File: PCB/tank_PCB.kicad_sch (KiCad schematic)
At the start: 60 parts, among them J1 TFT, J2 PTSA 1,5/ 2-3,5-Z, J3 PTSA 1,5/ 8-3,5-Z, J5 USB4110GFA, U1 ADS1115IDGS, U3 LM2735X (1.6MHz), U4 ESP32-C6-WROOM-1, U5 MCP1826S-3302E/DB

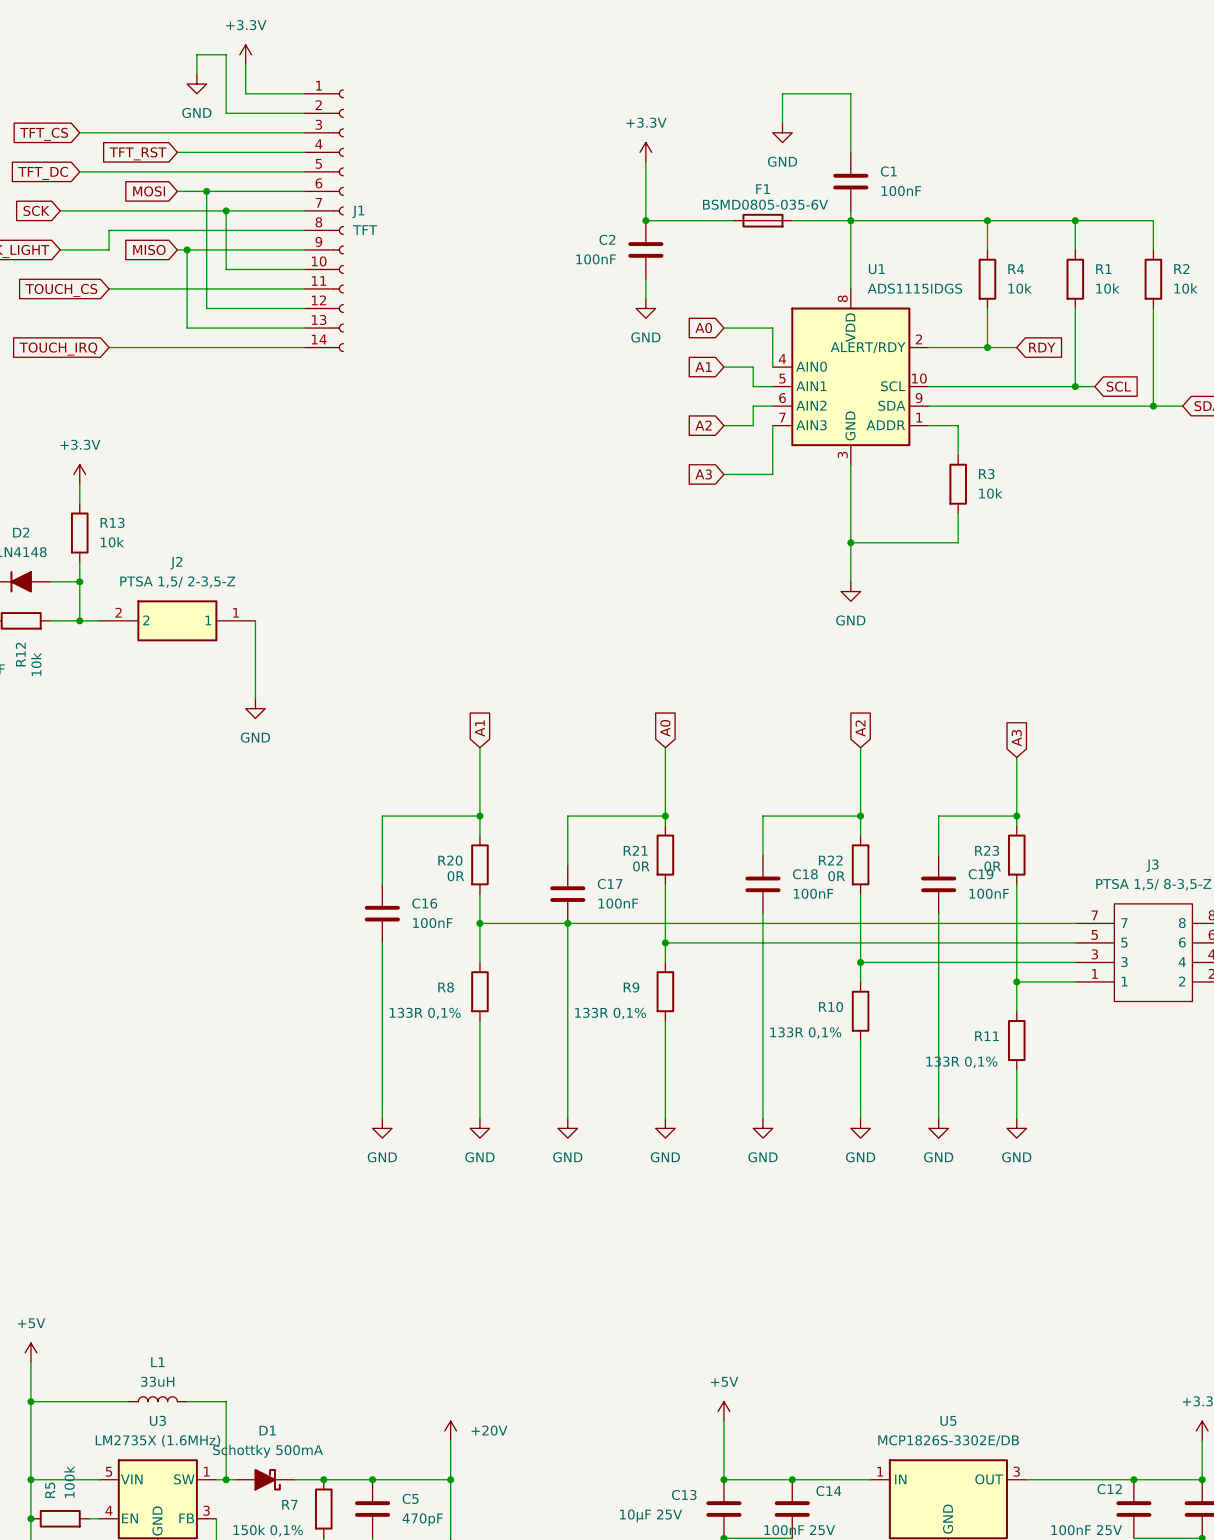
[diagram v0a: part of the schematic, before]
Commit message: Correcting PCB bug J3 pin 7 at GND
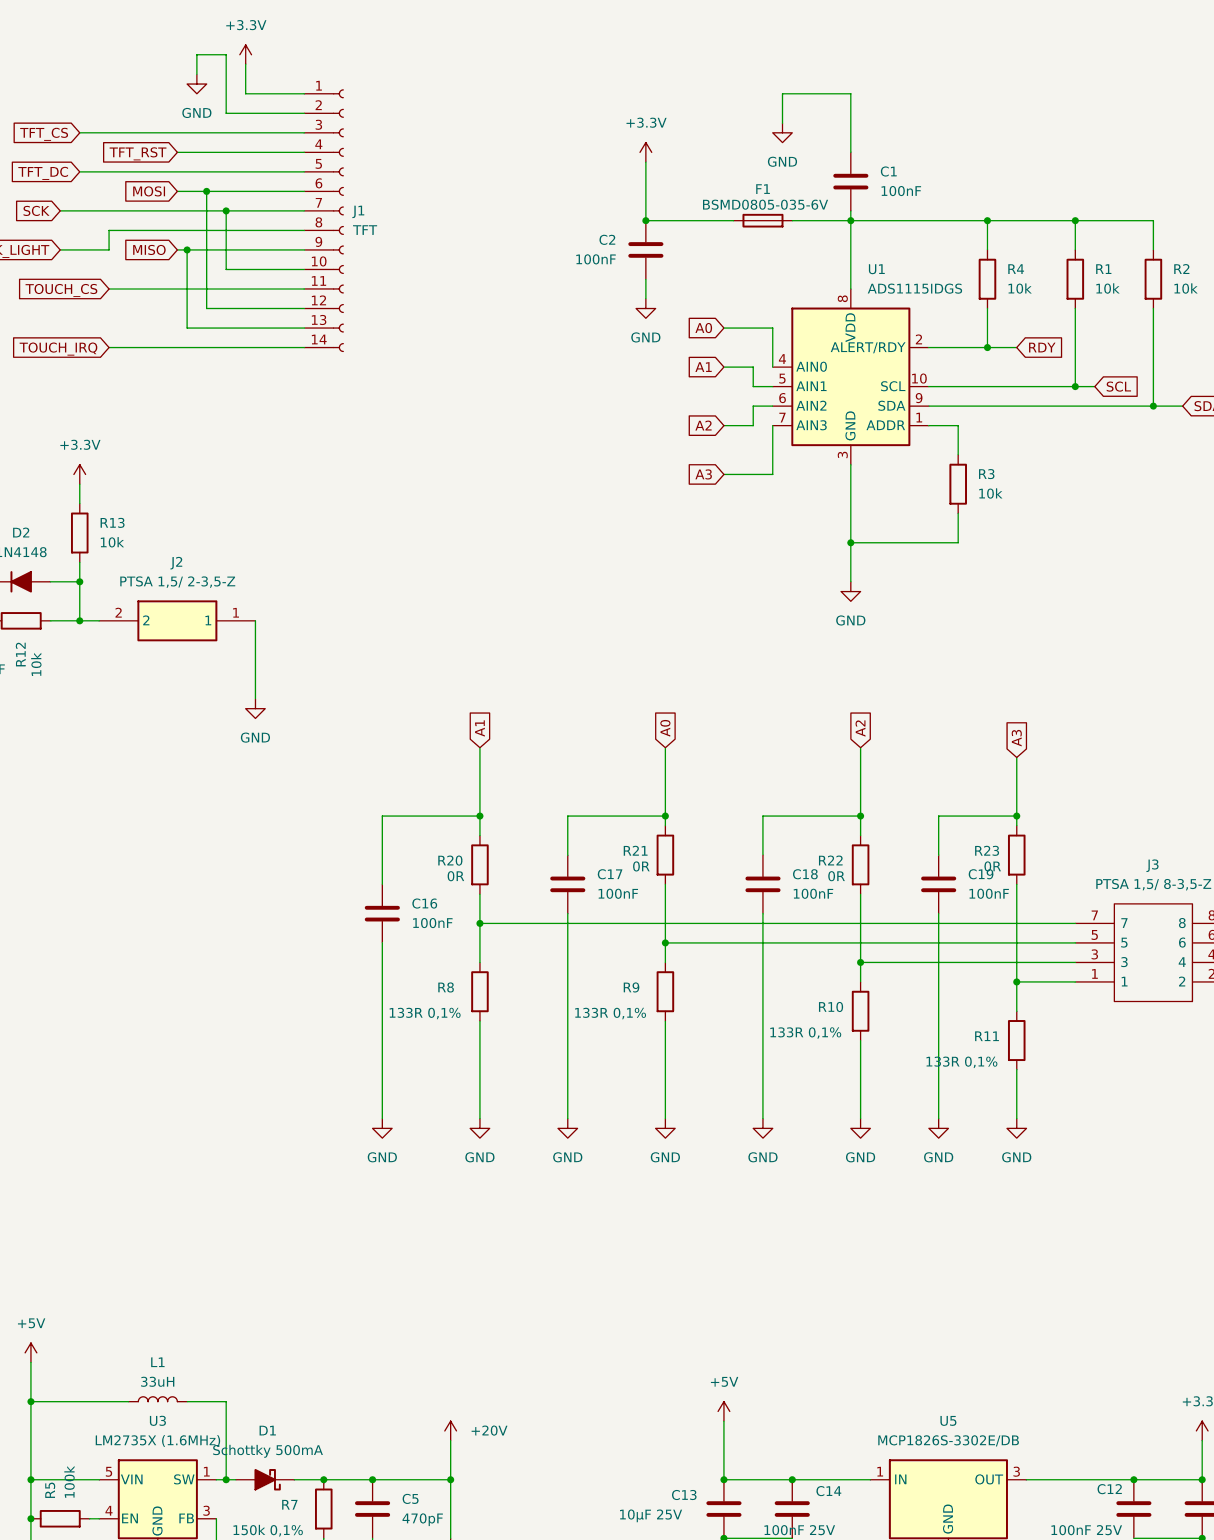
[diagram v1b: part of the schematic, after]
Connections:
- net GND: no longer J3.7, R20.2, R8.1
- new net: J3.7, R20.2, R8.1
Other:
- moved on the sheet: C17
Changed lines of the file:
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@@
 (kicad_sch
-	(version 20231120)
+	(version 20250114)
 	(generator "eeschema")
-	(generator_version "8.0")
+	(generator_version "9.0")
 	(paper "A3")
 	(junction
@@
 	)
 	(junction
-		(at 304.8 132.08)
-		(diameter 0)
-		(color 0 0 0 0)
-	)
-	(junction
 		(at 116.84 180.34)
 		(diameter 0)
@@
 	(wire
 		(pts
-			(xy 304.8 124.46) (xy 304.8 118.11)
+			(xy 304.8 123.19) (xy 304.8 118.11)
 		)
 		(stroke
@@
 	(wire
 		(pts
-			(xy 304.8 132.08) (xy 293.37 132.08)
-		)
-		(stroke
-			(width 0)
-			(type default)
-		)
-	)
-	(wire
-		(pts
 			(xy 128.27 194.31) (xy 128.27 198.12)
 		)
@@
 	(wire
 		(pts
-			(xy 370.84 132.08) (xy 304.8 132.08)
+			(xy 293.37 132.08) (xy 370.84 132.08)
 		)
 		(stroke
@@
 	(wire
 		(pts
-			(xy 304.8 132.08) (xy 304.8 157.48)
+			(xy 304.8 130.81) (xy 304.8 157.48)
 		)
 		(stroke
@@
 	(symbol
 		(lib_id "Device:C")
-		(at 304.8 128.27 0)
+		(at 304.8 127 0)
 		(unit 1)
 		(exclude_from_sim no)
@@
 		(fields_autoplaced yes)
 		(property "Reference" "C17"
-			(at 308.61 126.9999 0)
+			(at 308.61 125.7299 0)
 			(effects
 				(font
@@
 		)
 		(property "Value" "100nF"
-			(at 308.61 129.5399 0)
+			(at 308.61 128.2699 0)
 			(effects
 				(font
@@
 		)
 		(property "Footprint" "Capacitor_SMD:C_0805_2012Metric_Pad1.18x1.45mm_HandSolder"
-			(at 305.7652 132.08 0)
+			(at 305.7652 130.81 0)
 			(effects
 				(font
@@
 		)
 		(property "Datasheet" "~"
-			(at 304.8 128.27 0)
+			(at 304.8 127 0)
 			(effects
 				(font
@@
 		)
 		(property "Description" "Unpolarized capacitor"
-			(at 304.8 128.27 0)
+			(at 304.8 127 0)
 			(effects
 				(font
@@
 		)
 	)
+	(embedded_fonts no)
 )

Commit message: Clearing Kicad Warnings
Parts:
- J2: footprint Phoenix Contact PTSA 2:1985195 -> zTankFootprints:Phoenix Contact PTSA 2; symbol 1985195:1985195 -> Phoenix contact PTSA 2:1985195
- J3: footprint Phoenix Contact PTSA 8:1985250 -> zTankFootprints:Phoenix Contact PTSA 8; symbol 1985250:1985250 -> Phoenix contact PTSA 8:1985250
- J5: footprint GCT-USB4110GFA:GCT_USB4110GFA -> zTankFootprints:GCT_USB4110GFA; Description_1 USB-C (USB TYPE-C) USB 2.0 Receptacle Connector 24 (16+8 Dummy) Position Surface Mount, Right Angle -> USB-C (USB TYPE-C) USB 2.0 Receptacle Connector 24 (16+8 Dummy) Position Surface Mount, Right Angle
- S1: footprint CUI switch:SW_TS07-667-30-BK-100-SMT-TR -> zTankFootprints:CUI switch SW_TS07-667-30-BK-100-SMT-TR; Availability (none) -> In Stock; Check_prices (none) -> https://www.snapeda.com/parts/TS07-667-30-BK-100-SMT-TR/Sam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; Description_1 (none) -> 6 x 6.7 mm, 3 mm Actuator Height, 100 gf, Black, Surface Mo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; MF (none) -> Same Sky; MP (none) -> TS07-667-30-BK-100-SMT-TR; Package (none) -> None; Price (none) -> None; SnapEDA_Link (none) -> https://www.snapeda.com/parts/TS07-667-30-BK-100-SMT-TR/Sam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
- U4: footprint PCM_Espressif:ESP32-C6-WROOM-1 -> zTankFootprints:ESP32-C6-WROOM-1; symbol PCM_Espressif:ESP32-C6-WROOM-1 -> Espressif:ESP32-C6-WROOM-1
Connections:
- no-connect marks 7 -> 9
